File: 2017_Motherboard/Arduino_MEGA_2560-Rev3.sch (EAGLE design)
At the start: 93 parts, among them IC1 NCP1117ST50T3G, IC2 FT232RL, IC3 ATMEGA2560-16AU, IC4 MAX4312ESE, IC5 MAX3468CPA, IC7 LMV358IDGKR, X1 POWERSUPPLY_DC21MMX, Y1 CSTCE16M0V53-R0 16MHZ

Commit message: Motherboard routing
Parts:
- removed COMMUNICATION: 8x1F-H8.5, SmartPrj:PINHD-1X8
- removed XIO: 18x2F-H8.5, SmartPrj:PINHD-2X18
- added IC6: MAX4312ESE, maxim:MAX4312ESE
- added J9: (no value), SparkFun-Connectors:M02PTH
- added JP1: (no value), pinhead:PINHD-2X5
- added JP2: (no value), pinhead:PINHD-2X9
- added R31, R33: 0, SparkFun-Resistors:30.1KOHM1/10W1%(0603)
- added R32, R34: inf, SparkFun-Resistors:30.1KOHM1/10W1%(0603)
- added VIDEO_OUT1: A1944-50, con-coax:A1944-50
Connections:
- new net N$17: R31.2, R32.1
- new net N$18: R33.2, R34.1
- new net VIDEO_OUT1: IC6.OUT, R33.1, VIDEO_OUT1.1
- net +5V: now also IC4.!SHDN, IC6.!SHDN, IC6.V+, JP1.1, JP1.2; no longer XIO.1, XIO.2
- net GND: now also IC6.V-, JP2.17, JP2.18, R32.2, R34.2, VIDEO_OUT1.2; no longer IC4.!SHDN, IC4.FB, XIO.35, XIO.36
- net PA0: no longer XIO.3
- net PA1: no longer XIO.4
- net PA2: no longer XIO.5
- net PA3: now also IC6.A0; no longer XIO.6
- net PA4: now also IC6.A1; no longer XIO.7
- net PA5: now also IC6.A2; no longer XIO.8
- net PA6: no longer XIO.9
- net PA7: no longer XIO.10
- net PB0: now also JP2.16; no longer XIO.34
- net PB1: now also JP2.15; no longer XIO.33
- net PB2: now also JP2.14; no longer XIO.32
- net PB3: now also JP2.13; no longer XIO.31
- net PC0: now also JP1.10; no longer XIO.18
- net PC1: now also JP1.9; no longer XIO.17
- net PC2: now also JP1.8; no longer XIO.16
- net PC3: now also JP1.7; no longer XIO.15
- net PC4: now also JP1.6; no longer XIO.14
- net PC5: now also JP1.5; no longer XIO.13
- net PC6: now also JP1.4; no longer XIO.12
- net PC7: now also JP1.3; no longer XIO.11
- net PD7: now also JP2.1; no longer XIO.19
- net PG0: now also JP2.4; no longer XIO.22
- net PG1: now also JP2.3; no longer XIO.21
- net PG2: now also JP2.2; no longer XIO.20
- net PL0: now also JP2.12; no longer XIO.30
- net PL1: now also JP2.11; no longer XIO.29
- net PL2: now also JP2.10; no longer XIO.28
- net PL3: now also JP2.9; no longer XIO.27
- net PL4: now also JP2.8; no longer XIO.26
- net PL5: now also JP2.7; no longer XIO.25
- net PL6: now also JP2.6; no longer XIO.24
- net PL7: now also JP2.5; no longer XIO.23
- net RXD1: no longer COMMUNICATION.3
- net RXD2: no longer COMMUNICATION.5
- net RXD3: now also J9.1; no longer COMMUNICATION.7
- net SCL: no longer COMMUNICATION.1
- net SDA: no longer COMMUNICATION.2
- net TXD1: no longer COMMUNICATION.4
- net TXD2: no longer COMMUNICATION.6
- net TXD3: now also J9.2; no longer COMMUNICATION.8
- net VIDEO_OUT: now also R31.1
- net VID_0: now also IC6.IN0
- net VID_1: now also IC6.IN1
- net VID_2: now also IC6.IN2
- net VID_3: now also IC6.IN3
- net VID_4: now also IC6.IN4
- net VID_5: now also IC6.IN5
- net VID_6: now also IC6.IN6
- net VID_7: now also IC6.IN7
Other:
- note added: "PA0-7"
- note added: "RXD2"
- note added: "TXD2"
- note added: "Video Switching Redundant"
- note removed: "14"
- note removed: "15"
- note removed: "16"
- note removed: "17"
- note removed: "PA0"
- note removed: "PA1"
- note removed: "PA2"
- note removed: "PC0"
- note removed: "PC1"
- note removed: "PC2"
- moved on the sheet: VIDEO_OUT

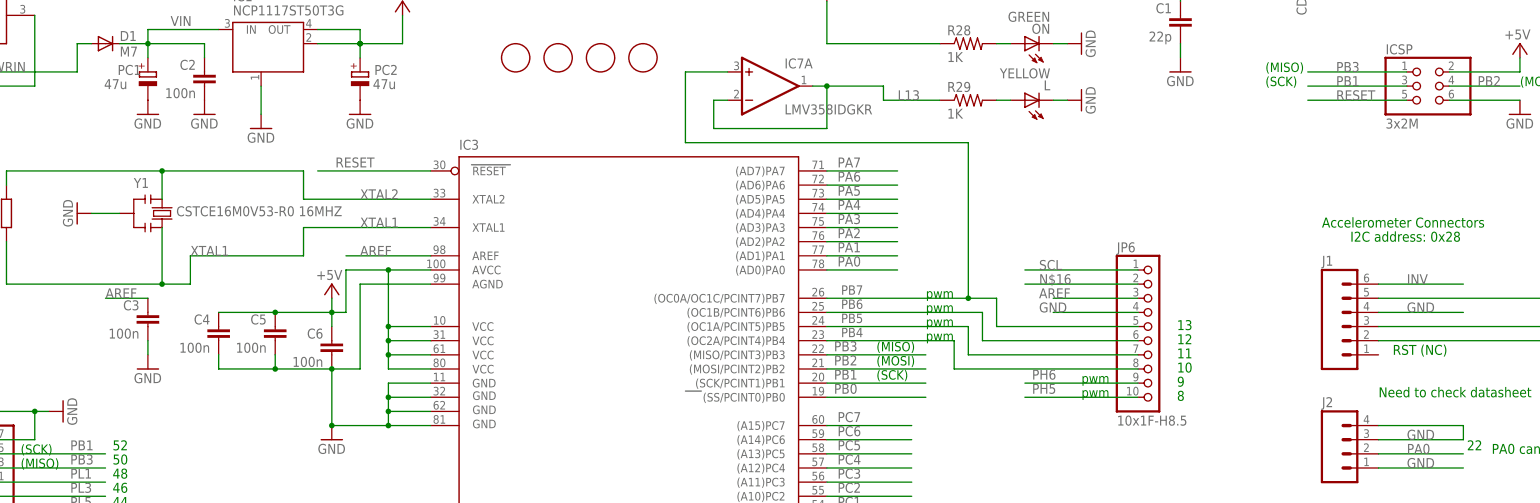
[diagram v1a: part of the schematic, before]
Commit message: Routed power
Working on AREF plane
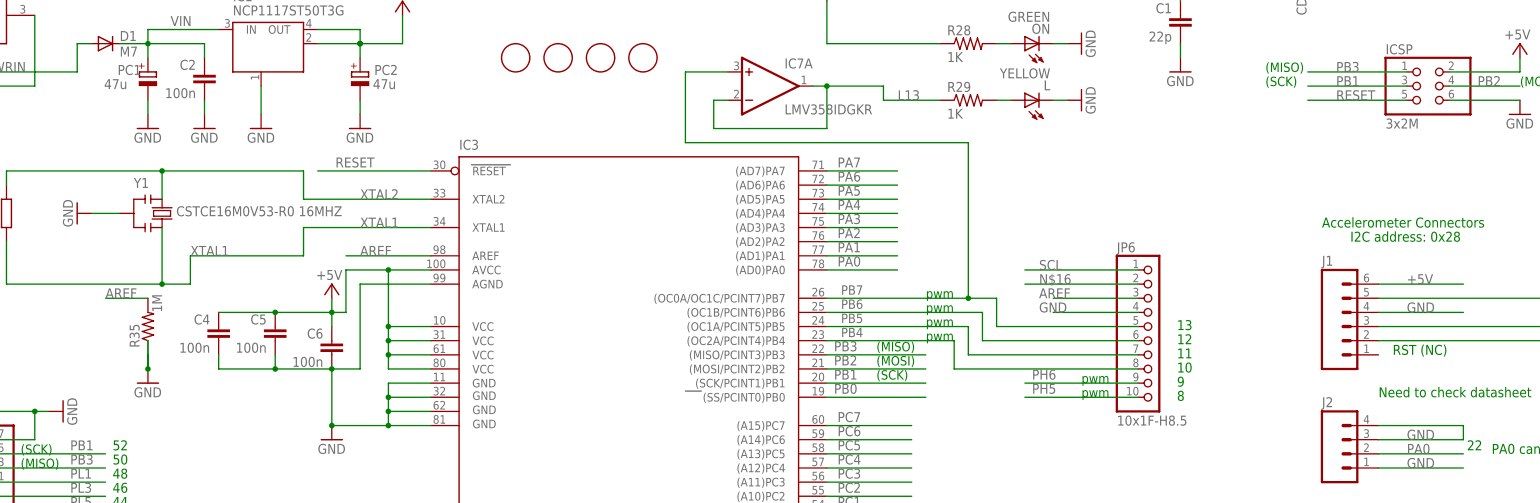
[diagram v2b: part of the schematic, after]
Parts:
- removed C3: 100n, SmartPrj:C-EU0603-RND
- added R35: (no value), SparkFun-Passives:RESISTOR0603-RES
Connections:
- removed net AGND: IC2.GND@A
- removed net INV: J1.6
- net +5V: now also J1.6
- net AREF: now also IC2.GND@A, R35.2; no longer C3.1
- net GND: now also R35.1; no longer C3.2
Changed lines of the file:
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@@
 <?xml version="1.0" encoding="utf-8"?>
 <!DOCTYPE eagle SYSTEM "eagle.dtd">
-<eagle version="7.6.0">
+<eagle version="7.7.0">
 <drawing>
 <settings>
@@
 <part name="GND10" library="supply1" deviceset="GND" device=""/>
 <part name="GND12" library="supply1" deviceset="GND" device=""/>
-<part name="GND19" library="supply1" deviceset="GND" device=""/>
+<part name="GND" library="supply1" deviceset="GND" device=""/>
 <part name="ON" library="led" deviceset="LED" device="CHIP-LED0805" value="GREEN"/>
 <part name="GND14" library="supply1" deviceset="GND" device=""/>
@@
 <part name="GND11" library="supply1" deviceset="GND" device=""/>
 <part name="IC1" library="linear" deviceset="MC33269ST*" device="" technology="-3.3T3" value="NCP1117ST50T3G"/>
-<part name="C3" library="SmartPrj" deviceset="C-EU" device="0603-RND" value="100n"/>
 <part name="GND8" library="supply1" deviceset="GND" device=""/>
 <part name="C6" library="SmartPrj" deviceset="C-EU" device="0603-RND" value="100n"/>
@@
 <part name="JP1" library="pinhead" deviceset="PINHD-2X5" device=""/>
 <part name="JP2" library="pinhead" deviceset="PINHD-2X9" device=""/>
+<part name="R35" library="SparkFun-Passives" deviceset="RESISTOR" device="0603-RES">
+<attribute name="R35" value="1M"/>
+</part>
 </parts>
 <sheets>
@@
 <attribute name="VALUE" x="19.685" y="25.4" size="1.778" layer="96" rot="R180"/>
 </instance>
-<instance part="GND7" gate="1" x="63.5" y="147.32"/>
+<instance part="GND7" gate="1" x="63.5" y="144.78"/>
 <instance part="PC1" gate="G$1" x="53.34" y="154.94" smashed="yes">
 <attribute name="NAME" x="47.879" y="154.4066" size="1.778" layer="95"/>
@@
 <attribute name="VALUE" x="93.726" y="151.8666" size="1.778" layer="96"/>
 </instance>
-<instance part="GND9" gate="1" x="53.34" y="147.32"/>
-<instance part="GND10" gate="1" x="91.44" y="147.32"/>
+<instance part="GND9" gate="1" x="53.34" y="144.78"/>
+<instance part="GND10" gate="1" x="91.44" y="144.78"/>
 <instance part="GND12" gate="1" x="43.18" y="-22.86" rot="R90"/>
-<instance part="GND19" gate="1" x="12.7" y="144.78"/>
+<instance part="GND" gate="1" x="12.7" y="144.78"/>
 <instance part="ON" gate="G$1" x="210.82" y="160.02" rot="R90"/>
 <instance part="GND14" gate="1" x="220.98" y="160.02" rot="R90"/>
@@
 <attribute name="VALUE" x="68.58" y="165.1" size="1.778" layer="96"/>
 </instance>
-<instance part="C3" gate="G$1" x="53.34" y="111.76" smashed="yes" rot="MR0">
-<attribute name="NAME" x="51.816" y="112.141" size="1.778" layer="95" rot="MR0"/>
-<attribute name="VALUE" x="51.816" y="107.061" size="1.778" layer="96" rot="MR0"/>
-</instance>
-<instance part="GND8" gate="1" x="53.34" y="101.6" smashed="yes">
-<attribute name="VALUE" x="50.8" y="99.06" size="1.778" layer="96"/>
+<instance part="GND8" gate="1" x="53.34" y="99.06" smashed="yes">
+<attribute name="VALUE" x="50.8" y="96.52" size="1.778" layer="96"/>
 </instance>
 <instance part="C6" gate="G$1" x="86.36" y="106.68" smashed="yes" rot="MR0">
@@
 <instance part="JP1" gate="A" x="22.86" y="55.88" rot="R180"/>
 <instance part="JP2" gate="A" x="22.86" y="78.74" rot="R180"/>
+<instance part="R35" gate="G$1" x="53.34" y="109.22" rot="R90">
+<attribute name="R35" x="55.88" y="111.76" size="1.778" layer="96" rot="R90"/>
+</instance>
 </instances>
 <busses>
@@
 <wire x1="492.76" y1="5.08" x2="459.74" y2="5.08" width="0.1524" layer="91"/>
 </segment>
+<segment>
+<pinref part="J1" gate="G$1" pin="6"/>
+<wire x1="274.32" y1="116.84" x2="289.56" y2="116.84" width="0.1524" layer="91"/>
+<label x="279.4" y="116.84" size="1.778" layer="95"/>
+</segment>
 </net>
 <net name="GND" class="2">
@@
 <pinref part="GND7" gate="1" pin="GND"/>
 <pinref part="C2" gate="G$1" pin="2"/>
+<wire x1="63.5" y1="147.32" x2="63.5" y2="149.86" width="0.1524" layer="91"/>
 </segment>
 <segment>
 <pinref part="PC2" gate="G$1" pin="-"/>
 <pinref part="GND10" gate="1" pin="GND"/>
+<wire x1="91.44" y1="147.32" x2="91.44" y2="149.86" width="0.1524" layer="91"/>
 </segment>
 <segment>
 <pinref part="GND9" gate="1" pin="GND"/>
 <pinref part="PC1" gate="G$1" pin="-"/>
+<wire x1="53.34" y1="147.32" x2="53.34" y2="149.86" width="0.1524" layer="91"/>
 </segment>
 <segment>
@@
 <junction x="12.7" y="152.4"/>
 <pinref part="X1" gate="G$1" pin="1"/>
-<pinref part="GND19" gate="1" pin="GND"/>
+<pinref part="GND" gate="1" pin="GND"/>
 <pinref part="X1" gate="G$1" pin="3"/>
 </segment>
@@
 </segment>
 <segment>
-<wire x1="53.34" y1="104.14" x2="53.34" y2="106.68" width="0.1524" layer="91"/>
-<pinref part="C3" gate="G$1" pin="2"/>
+<wire x1="53.34" y1="101.6" x2="53.34" y2="106.68" width="0.1524" layer="91"/>
 <pinref part="GND8" gate="1" pin="GND"/>
+<pinref part="R35" gate="G$1" pin="1"/>
+<junction x="53.34" y="101.6"/>
+<wire x1="53.34" y1="101.6" x2="53.34" y2="104.14" width="0.1524" layer="91"/>
 </segment>
 <segment>
@@
 <wire x1="53.34" y1="114.3" x2="45.72" y2="114.3" width="0.1524" layer="91"/>
 <label x="45.72" y="114.3" size="1.778" layer="95"/>
-<pinref part="C3" gate="G$1" pin="1"/>
+<pinref part="R35" gate="G$1" pin="2"/>
+</segment>
+<segment>
+<pinref part="IC2" gate="1" pin="GND@A"/>
+<wire x1="175.26" y1="-101.6" x2="170.18" y2="-101.6" width="0.1524" layer="91"/>
+<pinref part="U$1" gate="G$1" pin="AGND"/>
+<wire x1="170.18" y1="-101.6" x2="170.18" y2="-119.38" width="0.1524" layer="91"/>
 </segment>
 </net>
@@
 </segment>
 </net>
-<net name="INV" class="0">
-<segment>
-<pinref part="J1" gate="G$1" pin="6"/>
-<wire x1="274.32" y1="116.84" x2="289.56" y2="116.84" width="0.1524" layer="91"/>
-<label x="279.4" y="116.84" size="1.778" layer="95"/>
-</segment>
-</net>
 <net name="ADC11" class="0">
 <segment>
@@
 </segment>
 </net>
-<net name="AGND" class="0">
-<segment>
-<pinref part="IC2" gate="1" pin="GND@A"/>
-<wire x1="175.26" y1="-101.6" x2="170.18" y2="-101.6" width="0.1524" layer="91"/>
-<pinref part="U$1" gate="G$1" pin="AGND"/>
-<wire x1="170.18" y1="-101.6" x2="170.18" y2="-119.38" width="0.1524" layer="91"/>
-</segment>
-</net>

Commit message: Half of routing done
fixed errors in ERC, removed op amp on pin 13, disconnected AREF and
changed to AGND. AGND separated from GND by 1M resistor. Video routing
TBD. AGND plane TBD?
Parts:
- removed IC7: LMV358IDGKR, linear:LMV358MMX
- removed L: YELLOW, led:LEDCHIP-LED0805
- removed R29: 1K, SparkFun-Resistors:1KOHM-1/10W-1%(0603)
- removed R35: (no value), SparkFun-Passives:RESISTOR0603-RES
- added U$2: 1M, SparkFun-Resistors:820KOHM-1/10W-1%(0603)
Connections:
- removed net L13: IC7A.-IN, IC7A.OUT, R29.1
- removed net N$16: JP6.2
- removed net N$2: L.A, R29.2
- new net AGND: C4.2, C5.2, C6.2, IC2.GND@A, IC3.AGND, U$2.2
- net AREF: no longer IC2.GND@A, R35.2
- net GND: now also U$2.1; no longer C4.2, C5.2, C6.2, IC3.AGND, L.C, R35.1
- net N$17: now also IC4.FB
- net N$18: now also IC6.FB
- net PB7: no longer IC7A.+IN
- net SDA: now also JP6.2
